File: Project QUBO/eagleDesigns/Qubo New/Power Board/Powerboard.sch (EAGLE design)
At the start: 45 parts, among them IC1 PCF8574T, U1 UEI15

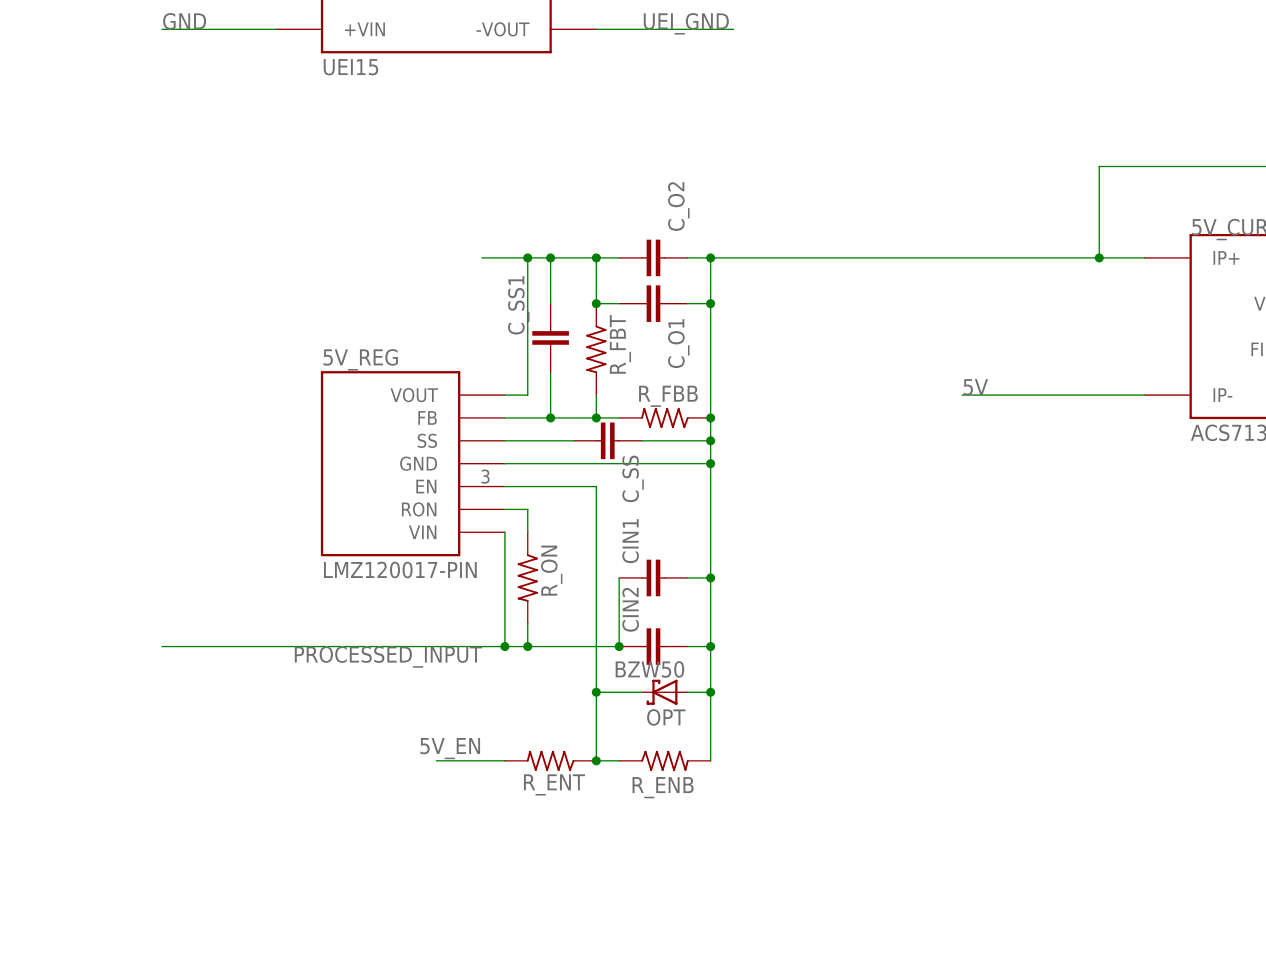
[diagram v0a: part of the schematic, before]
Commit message: 
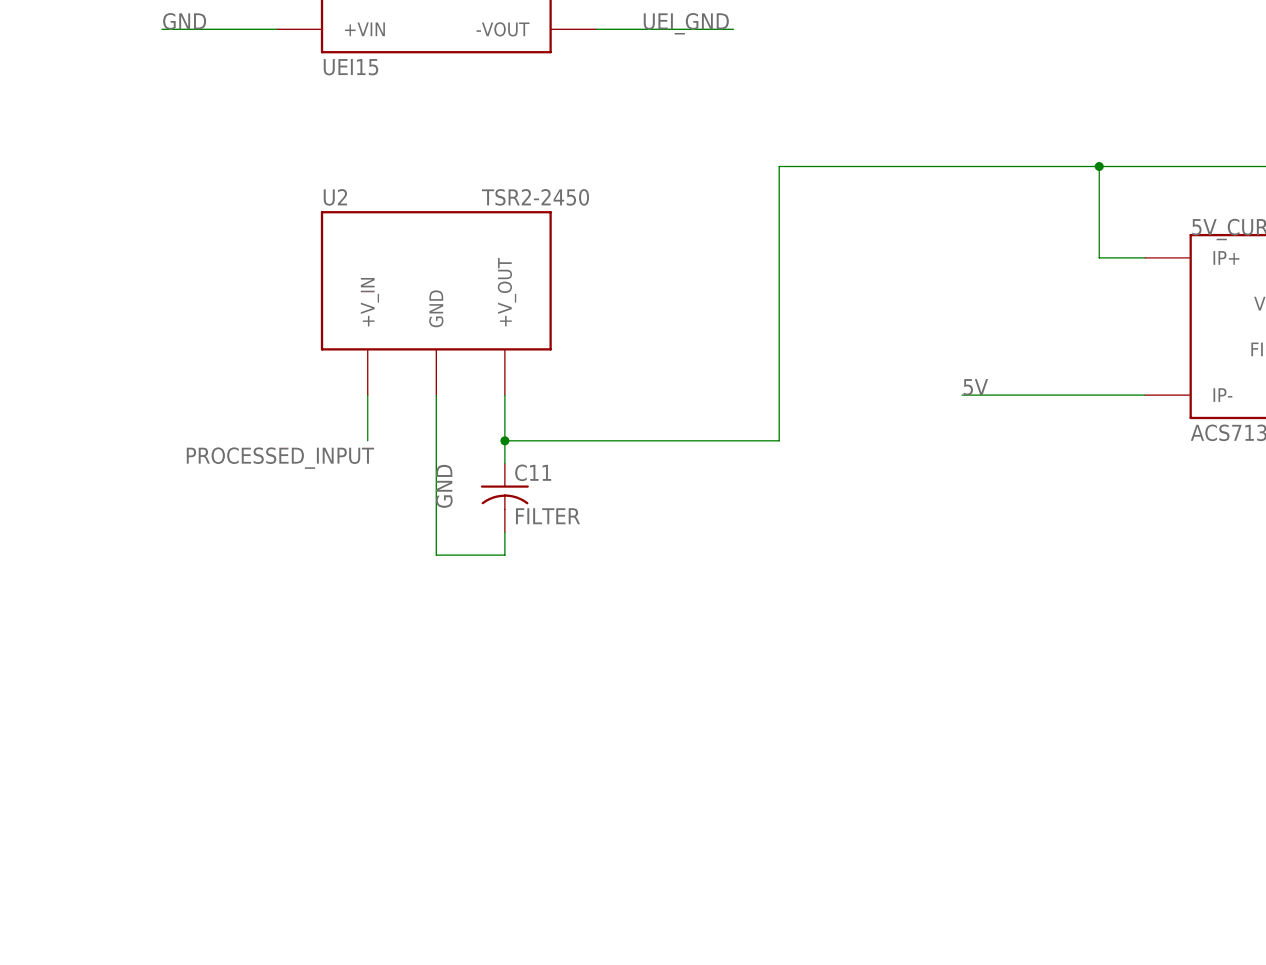
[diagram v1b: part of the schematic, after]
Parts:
- removed 5V_REG: LMZ120017-PIN, texas:LMZ120017-PIN
- removed CIN1, CIN2, C_O1, C_O2, C_SS, C_SS1: (no value), capacitor-wima:C5/3.5
- removed OPT: BZW50, diode:BZW50
- removed R_ENB, R_ENT, R_FBB, R_FBT, R_ON: (no value), resistor:R-US_R0805
- added C11: FILTER, resistor:C-USC0805
- added U2: TSR2-2450, tracoPower:TSR2-2450
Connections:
- removed net N$12: 5V_REG.RON, R_ON.1
- removed net N$13: 5V_REG.SS, C_SS.2
- removed net N$15: 5V_REG.VOUT, C_O1.2, C_O2.2, C_SS1.1, R_FBT.1
- removed net N$16: 5V_REG.EN, OPT.C, R_ENB.1, R_ENT.1
- removed net N$17: 5V_REG.FB, C_SS1.2, R_FBB.2, R_FBT.2
- new net N$4: 5V_CURRENT_SENSOR.IP+, 5V_CURRENT_SENSOR.VCC, C11.1, C9.2, U2.+V_OUT
- net 5V_EN: no longer R_ENT.2
- net GND: now also C11.2, U2.GND
- net PROCESSED_INPUT: now also U2.+V_IN; no longer 5V_CURRENT_SENSOR.IP+, 5V_CURRENT_SENSOR.VCC, 5V_REG.GND, 5V_REG.VIN, C9.2, CIN1.1, CIN1.2, CIN2.1, CIN2.2, C_O1.1, C_O2.1, C_SS.1, OPT.A, R_ENB.2, R_FBB.1, R_ON.2

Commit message: Capacitor and Powerboard
Added capacitor package and adjusted powerboard
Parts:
- C5: value XXX -> (none); device resistor:C-USC0805 -> resistor:CPOL-US
- C6: value 330u -> (none); device resistor:C-USC0805 -> resistor:CPOL-US
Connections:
- net 10V_OUT: now also C6.+; no longer C6.1
- net GND: now also C5.-, C6.-; no longer C5.2, C6.2
- net PROCESSED_INPUT: now also C5.+; no longer C5.1
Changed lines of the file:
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@@
 <?xml version="1.0" encoding="utf-8"?>
 <!DOCTYPE eagle SYSTEM "eagle.dtd">
-<eagle version="8.3.2">
+<eagle version="8.7.1">
 <drawing>
 <settings>
@@
 <layers>
 <layer number="1" name="Top" color="4" fill="1" visible="no" active="no"/>
+<layer number="2" name="Route2" color="1" fill="3" visible="no" active="no"/>
+<layer number="3" name="Route3" color="4" fill="3" visible="no" active="no"/>
+<layer number="4" name="Route4" color="1" fill="4" visible="no" active="no"/>
+<layer number="5" name="Route5" color="4" fill="4" visible="no" active="no"/>
+<layer number="6" name="Route6" color="1" fill="8" visible="no" active="no"/>
+<layer number="7" name="Route7" color="4" fill="8" visible="no" active="no"/>
+<layer number="8" name="Route8" color="1" fill="2" visible="no" active="no"/>
+<layer number="9" name="Route9" color="4" fill="2" visible="no" active="no"/>
+<layer number="10" name="Route10" color="1" fill="7" visible="no" active="no"/>
+<layer number="11" name="Route11" color="4" fill="7" visible="no" active="no"/>
+<layer number="12" name="Route12" color="1" fill="5" visible="no" active="no"/>
+<layer number="13" name="Route13" color="4" fill="5" visible="no" active="no"/>
+<layer number="14" name="Route14" color="1" fill="6" visible="no" active="no"/>
+<layer number="15" name="Route15" color="4" fill="6" visible="no" active="no"/>
 <layer number="16" name="Bottom" color="1" fill="1" visible="no" active="no"/>
 <layer number="17" name="Pads" color="2" fill="1" visible="no" active="no"/>
@@
 <part name="10V_REGULATOR" library="texas" deviceset="PTN" device="78020"/>
 <part name="ADJUST" library="resistor" deviceset="R-US_" device="R0805" value="2.66k"/>
-<part name="C6" library="resistor" deviceset="C-US" device="C0805" value="330u"/>
-<part name="C5" library="resistor" deviceset="C-US" device="C0805" value="XXX"/>
 <part name="10V_CURRENT_SENSOR" library="allegro" deviceset="ACS713" device="SOIC"/>
 <part name="C7" library="resistor" deviceset="C-US" device="C0805" value="0.1u"/>
@@
 <part name="U2" library="tracoPower" deviceset="TSR2-2450" device=""/>
 <part name="C11" library="resistor" deviceset="C-US" device="C0805" value="FILTER"/>
+<part name="C5" library="resistor" deviceset="CPOL-US" device=""/>
+<part name="C6" library="resistor" deviceset="CPOL-US" device=""/>
 </parts>
 <sheets>
@@
 <instance part="10V_REGULATOR" gate="G$1" x="83.82" y="-71.12"/>
 <instance part="ADJUST" gate="G$1" x="88.9" y="-88.9"/>
-<instance part="C6" gate="G$1" x="114.3" y="-78.74"/>
-<instance part="C5" gate="G$1" x="48.26" y="-68.58" rot="R270"/>
 <instance part="10V_CURRENT_SENSOR" gate="G$1" x="160.02" y="-78.74"/>
 <instance part="C7" gate="G$1" x="187.96" y="-71.12" rot="R270"/>
@@
 <instance part="U2" gate="U1" x="-119.38" y="-40.64"/>
 <instance part="C11" gate="G$1" x="-111.76" y="-63.5"/>
+<instance part="C5" gate="G$1" x="48.26" y="-68.58" rot="R270"/>
+<instance part="C6" gate="G$1" x="114.3" y="-78.74"/>
 </instances>
 <busses>
@@
 <pinref part="10V_REGULATOR" gate="G$1" pin="GND1"/>
 <label x="55.88" y="-63.5" size="1.778" layer="95"/>
-<pinref part="C5" gate="G$1" pin="2"/>
 <wire x1="43.18" y1="-68.58" x2="38.1" y2="-68.58" width="0.1524" layer="91"/>
 <wire x1="38.1" y1="-68.58" x2="38.1" y2="-63.5" width="0.1524" layer="91"/>
 <wire x1="38.1" y1="-63.5" x2="68.58" y2="-63.5" width="0.1524" layer="91"/>
+<pinref part="C5" gate="G$1" pin="-"/>
 </segment>
 <segment>
@@
 <wire x1="101.6" y1="-76.2" x2="101.6" y2="-88.9" width="0.1524" layer="91"/>
 <wire x1="101.6" y1="-88.9" x2="114.3" y2="-88.9" width="0.1524" layer="91"/>
-<pinref part="C6" gate="G$1" pin="2"/>
 <wire x1="114.3" y1="-88.9" x2="114.3" y2="-83.82" width="0.1524" layer="91"/>
 <pinref part="ADJUST" gate="G$1" pin="2"/>
@@
 <junction x="101.6" y="-88.9"/>
 <label x="104.14" y="-88.9" size="1.778" layer="95"/>
+<pinref part="C6" gate="G$1" pin="-"/>
 </segment>
 <segment>
@@
 <wire x1="68.58" y1="-68.58" x2="50.8" y2="-68.58" width="0.1524" layer="91"/>
 <label x="55.88" y="-68.58" size="1.778" layer="95"/>
-<pinref part="C5" gate="G$1" pin="1"/>
+<pinref part="C5" gate="G$1" pin="+"/>
 </segment>
 <segment>
@@
 <wire x1="99.06" y1="-66.04" x2="114.3" y2="-66.04" width="0.1524" layer="91"/>
 <wire x1="114.3" y1="-66.04" x2="114.3" y2="-71.12" width="0.1524" layer="91"/>
-<pinref part="C6" gate="G$1" pin="1"/>
 <junction x="114.3" y="-66.04"/>
 <label x="99.06" y="-71.12" size="1.778" layer="95"/>
 <pinref part="10V_CURRENT_SENSOR" gate="G$1" pin="IP+"/>
 <wire x1="147.32" y1="-71.12" x2="114.3" y2="-71.12" width="0.1524" layer="91"/>
-</segment>
-</net>
+<pinref part="C6" gate="G$1" pin="+"/>
+</segment>
+</net>

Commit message: this power board should be fixed
I had to fix anthony's screwed up board
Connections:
- removed net UEI_INPUT: U1.-VIN, UWE_CURRENT_SENSOR.IP-
- new net N$6: U1.+VIN, UWE_CURRENT_SENSOR.IP-
- net GND: now also U1.-VIN; no longer U1.+VIN
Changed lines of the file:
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@@
 <?xml version="1.0" encoding="utf-8"?>
 <!DOCTYPE eagle SYSTEM "eagle.dtd">
-<eagle version="8.7.1">
+<eagle version="8.6.0">
 <drawing>
 <settings>
@@
 </segment>
 <segment>
-<pinref part="U1" gate="U1" pin="+VIN"/>
-<wire x1="-137.16" y1="-12.7" x2="-149.86" y2="-12.7" width="0.1524" layer="91"/>
-<label x="-149.86" y="-12.7" size="1.778" layer="95"/>
-</segment>
-<segment>
 <pinref part="10V_OUT" gate="U1" pin="P$1"/>
 <wire x1="132.08" y1="20.32" x2="121.92" y2="20.32" width="0.1524" layer="91"/>
@@
 <wire x1="-111.76" y1="-71.12" x2="-119.38" y2="-71.12" width="0.1524" layer="91"/>
 <wire x1="-119.38" y1="-71.12" x2="-119.38" y2="-53.34" width="0.1524" layer="91"/>
+</segment>
+<segment>
+<pinref part="U1" gate="U1" pin="-VIN"/>
+<wire x1="-137.16" y1="2.54" x2="-149.86" y2="2.54" width="0.1524" layer="91"/>
 </segment>
 </net>
@@
 <wire x1="58.42" y1="30.48" x2="43.18" y2="30.48" width="0.1524" layer="91"/>
 <label x="40.64" y="30.48" size="1.778" layer="95"/>
-</segment>
-</net>
-<net name="UEI_INPUT" class="0">
-<segment>
-<pinref part="UWE_CURRENT_SENSOR" gate="G$1" pin="IP-"/>
-<wire x1="-137.16" y1="17.78" x2="-149.86" y2="17.78" width="0.1524" layer="91"/>
-<label x="-149.86" y="17.78" size="1.778" layer="95"/>
-<pinref part="U1" gate="U1" pin="-VIN"/>
-<wire x1="-137.16" y1="2.54" x2="-149.86" y2="2.54" width="0.1524" layer="91"/>
-<wire x1="-149.86" y1="2.54" x2="-149.86" y2="17.78" width="0.1524" layer="91"/>
 </segment>
 </net>
@@
 </segment>
 </net>
+<net name="N$6" class="0">
+<segment>
+<pinref part="U1" gate="U1" pin="+VIN"/>
+<wire x1="-137.16" y1="-12.7" x2="-157.48" y2="-12.7" width="0.1524" layer="91"/>
+<wire x1="-157.48" y1="-12.7" x2="-157.48" y2="17.78" width="0.1524" layer="91"/>
+<pinref part="UWE_CURRENT_SENSOR" gate="G$1" pin="IP-"/>
+<wire x1="-157.48" y1="17.78" x2="-137.16" y2="17.78" width="0.1524" layer="91"/>
+</segment>
+</net>

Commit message: Fix to powerboard
Minor errors corrected to power board
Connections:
- removed net 5V_EN: IC1.P1
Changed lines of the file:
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@@
 <pinref part="U1" gate="U1" pin="-VIN"/>
 <wire x1="-137.16" y1="2.54" x2="-149.86" y2="2.54" width="0.1524" layer="91"/>
+<label x="-149.86" y="2.54" size="1.778" layer="95"/>
 </segment>
 </net>
@@
 <wire x1="58.42" y1="25.4" x2="43.18" y2="25.4" width="0.1524" layer="91"/>
 <label x="40.64" y="25.4" size="1.778" layer="95"/>
-</segment>
-</net>
-<net name="5V_EN" class="0">
-<segment>
-<pinref part="IC1" gate="G$1" pin="P1"/>
-<wire x1="7.62" y1="38.1" x2="12.7" y2="38.1" width="0.1524" layer="91"/>
-<label x="10.16" y="38.1" size="1.778" layer="95"/>
 </segment>
 </net>
@@
 </sheet>
 </sheets>
+<errors>
+</errors>
 </schematic>
 </drawing>
